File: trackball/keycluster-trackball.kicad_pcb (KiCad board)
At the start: 2 copper layers, 15 x 13.2 mm, 7 parts, among them P8 CONN_7, U1 TLE4964-5M, U2 TLE4964-5M, U3 TLE4964-5M, U4 TLE4964-5M

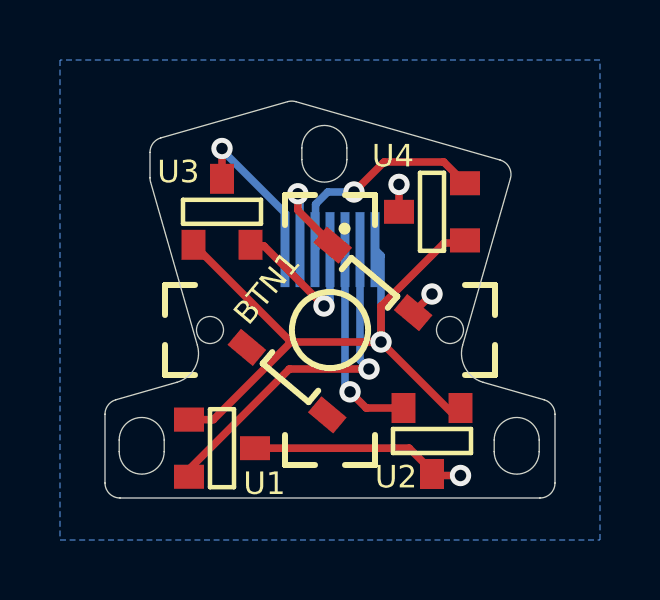
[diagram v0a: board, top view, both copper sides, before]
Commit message: Replace the TL3315NF250Q module with TL3315NFxxxQ and use TL3315NF100Q as the part value to describe the actual part name.
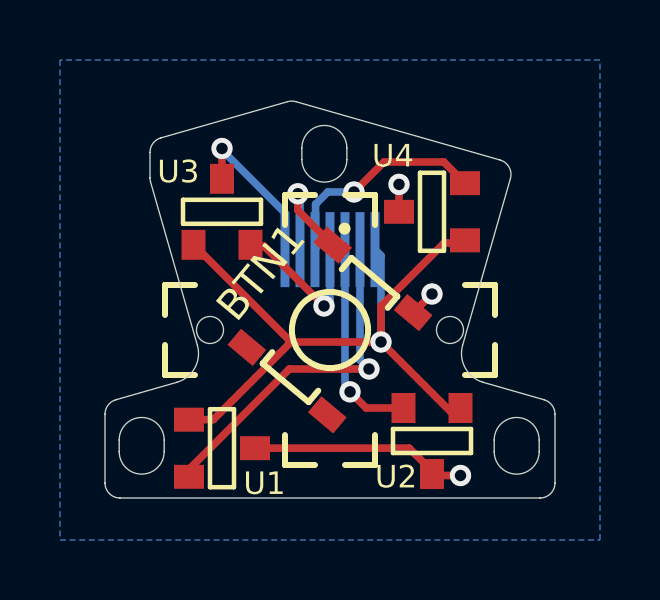
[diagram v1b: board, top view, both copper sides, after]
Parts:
- BTN1: value BTN -> TL3315NF100Q; footprint UGL:TL3315NF250Q -> UGL:TL3315NFxxxQ
- U1, U2, U3, U4: value TLE4964-5M -> TLE49681MXTSA1
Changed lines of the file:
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@@
       (effects (font (size 0.75 0.75) (thickness 0.15)))
     )
-    (fp_text value TLE4964-5M (at 0 -2.667) (layer F.SilkS) hide
+    (fp_text value TLE49681MXTSA1 (at 0 -2.667) (layer F.SilkS) hide
       (effects (font (size 0.75 0.75) (thickness 0.15)))
     )
+    (fp_line (start -1.3 0.4) (end 1.3 0.4) (layer F.SilkS) (width 0.15))
+    (fp_line (start 1.3 -0.4) (end -1.3 -0.4) (layer F.SilkS) (width 0.15))
+    (fp_line (start 1.3 -0.4) (end 1.3 0.4) (layer F.SilkS) (width 0.15))
     (fp_line (start -1.3 -0.4) (end -1.3 0.4) (layer F.SilkS) (width 0.15))
-    (fp_line (start 1.3 -0.4) (end 1.3 0.4) (layer F.SilkS) (width 0.15))
-    (fp_line (start 1.3 -0.4) (end -1.3 -0.4) (layer F.SilkS) (width 0.15))
-    (fp_line (start -1.3 0.4) (end 1.3 0.4) (layer F.SilkS) (width 0.15))
     (pad 1 smd rect (at -0.9525 1.09982) (size 0.8001 1.00076) (layers F.Cu F.Paste F.Mask)
       (net 4 +3V3))
@@
       (effects (font (size 0.75 0.75) (thickness 0.15)))
     )
-    (fp_text value TLE4964-5M (at 0 -2.667 90) (layer F.SilkS) hide
+    (fp_text value TLE49681MXTSA1 (at 0 -2.667 90) (layer F.SilkS) hide
       (effects (font (size 0.75 0.75) (thickness 0.15)))
     )
+    (fp_line (start -1.3 0.4) (end 1.3 0.4) (layer F.SilkS) (width 0.15))
+    (fp_line (start 1.3 -0.4) (end -1.3 -0.4) (layer F.SilkS) (width 0.15))
+    (fp_line (start 1.3 -0.4) (end 1.3 0.4) (layer F.SilkS) (width 0.15))
     (fp_line (start -1.3 -0.4) (end -1.3 0.4) (layer F.SilkS) (width 0.15))
-    (fp_line (start 1.3 -0.4) (end 1.3 0.4) (layer F.SilkS) (width 0.15))
-    (fp_line (start 1.3 -0.4) (end -1.3 -0.4) (layer F.SilkS) (width 0.15))
-    (fp_line (start -1.3 0.4) (end 1.3 0.4) (layer F.SilkS) (width 0.15))
     (pad 1 smd rect (at -0.9525 1.09982 90) (size 0.8001 1.00076) (layers F.Cu F.Paste F.Mask)
       (net 4 +3V3))
@@
       (effects (font (size 0.75 0.75) (thickness 0.15)))
     )
-    (fp_text value TLE4964-5M (at 0 -2.667) (layer F.SilkS) hide
+    (fp_text value TLE49681MXTSA1 (at 0 -2.667) (layer F.SilkS) hide
       (effects (font (size 0.75 0.75) (thickness 0.15)))
     )
+    (fp_line (start -1.3 0.4) (end 1.3 0.4) (layer F.SilkS) (width 0.15))
+    (fp_line (start 1.3 -0.4) (end -1.3 -0.4) (layer F.SilkS) (width 0.15))
+    (fp_line (start 1.3 -0.4) (end 1.3 0.4) (layer F.SilkS) (width 0.15))
     (fp_line (start -1.3 -0.4) (end -1.3 0.4) (layer F.SilkS) (width 0.15))
-    (fp_line (start 1.3 -0.4) (end 1.3 0.4) (layer F.SilkS) (width 0.15))
-    (fp_line (start 1.3 -0.4) (end -1.3 -0.4) (layer F.SilkS) (width 0.15))
-    (fp_line (start -1.3 0.4) (end 1.3 0.4) (layer F.SilkS) (width 0.15))
     (pad 1 smd rect (at -0.9525 1.09982 180) (size 0.8001 1.00076) (layers F.Cu F.Paste F.Mask)
       (net 4 +3V3))
@@
       (effects (font (size 0.75 0.75) (thickness 0.15)))
     )
-    (fp_text value TLE4964-5M (at 0 -2.667 90) (layer F.SilkS) hide
+    (fp_text value TLE49681MXTSA1 (at 0 -2.667 90) (layer F.SilkS) hide
       (effects (font (size 0.75 0.75) (thickness 0.15)))
     )
+    (fp_line (start -1.3 -0.4) (end -1.3 0.4) (layer F.SilkS) (width 0.15))
+    (fp_line (start 1.3 -0.4) (end 1.3 0.4) (layer F.SilkS) (width 0.15))
+    (fp_line (start 1.3 -0.4) (end -1.3 -0.4) (layer F.SilkS) (width 0.15))
     (fp_line (start -1.3 0.4) (end 1.3 0.4) (layer F.SilkS) (width 0.15))
-    (fp_line (start 1.3 -0.4) (end -1.3 -0.4) (layer F.SilkS) (width 0.15))
-    (fp_line (start 1.3 -0.4) (end 1.3 0.4) (layer F.SilkS) (width 0.15))
-    (fp_line (start -1.3 -0.4) (end -1.3 0.4) (layer F.SilkS) (width 0.15))
     (pad 3 smd rect (at 0 -1.09982 270) (size 0.8001 1.00076) (layers F.Cu F.Paste F.Mask)
       (net 1 GND))
@@
       (effects (font (size 1 1) (thickness 0.15)))
     )
+    (fp_circle (center 0 0) (end 1.5 0) (layer Cmts.User) (width 0.2))
+    (fp_line (start 1.5 -4.5) (end -1.5 -4.5) (layer Cmts.User) (width 0.2))
+    (fp_line (start -1.5 -4.5) (end -1.5 -1.5) (layer Cmts.User) (width 0.2))
+    (fp_line (start -1.5 -1.5) (end -5.5 -1.5) (layer Cmts.User) (width 0.2))
+    (fp_line (start -5.5 -1.5) (end -5.5 1.5) (layer Cmts.User) (width 0.2))
+    (fp_line (start -5.5 1.5) (end -1.5 1.5) (layer Cmts.User) (width 0.2))
+    (fp_line (start -1.5 1.5) (end -1.5 4.5) (layer Cmts.User) (width 0.2))
+    (fp_line (start -1.5 4.5) (end 1.5 4.5) (layer Cmts.User) (width 0.2))
+    (fp_line (start 1.5 4.5) (end 1.5 1.5) (layer Cmts.User) (width 0.2))
+    (fp_line (start 1.5 1.5) (end 5.5 1.5) (layer Cmts.User) (width 0.2))
+    (fp_line (start 5.5 1.5) (end 5.5 -1.5) (layer Cmts.User) (width 0.2))
+    (fp_line (start 5.5 -1.5) (end 1.5 -1.5) (layer Cmts.User) (width 0.2))
+    (fp_line (start 1.5 -1.5) (end 1.5 -4.5) (layer Cmts.User) (width 0.2))
+    (fp_line (start -1.5 -3) (end -2 -3) (layer Cmts.User) (width 0.2))
+    (fp_line (start -1.5 -4) (end -2 -4) (layer Cmts.User) (width 0.2))
+    (fp_line (start 1.5 4) (end 2 4) (layer Cmts.User) (width 0.2))
+    (fp_line (start 1.5 3) (end 2 3) (layer Cmts.User) (width 0.2))
+    (fp_line (start 3 -1.5) (end 3 -2) (layer Cmts.User) (width 0.2))
+    (fp_line (start 4 -1.5) (end 4 -2) (layer Cmts.User) (width 0.2))
+    (fp_line (start -3 1.5) (end -3 2) (layer Cmts.User) (width 0.2))
+    (fp_line (start -4 1.5) (end -4 2) (layer Cmts.User) (width 0.2))
+    (fp_line (start -5.5 -1.5) (end -4.5 -1.5) (layer F.SilkS) (width 0.2))
+    (fp_line (start -5.5 -0.5) (end -5.5 -1.5) (layer F.SilkS) (width 0.2))
+    (fp_line (start -5.5 1.5) (end -5.5 0.5) (layer F.SilkS) (width 0.2))
+    (fp_line (start -4.5 1.5) (end -5.5 1.5) (layer F.SilkS) (width 0.2))
+    (fp_line (start 5.5 1.5) (end 4.5 1.5) (layer F.SilkS) (width 0.2))
+    (fp_line (start 5.5 0.5) (end 5.5 1.5) (layer F.SilkS) (width 0.2))
+    (fp_line (start -1.5 -4.5) (end -0.5 -4.5) (layer F.SilkS) (width 0.2))
+    (fp_line (start -1.5 -3.5) (end -1.5 -4.5) (layer F.SilkS) (width 0.2))
+    (fp_line (start 1.5 -4.5) (end 1.5 -3.5) (layer F.SilkS) (width 0.2))
+    (fp_line (start 0.5 -4.5) (end 1.5 -4.5) (layer F.SilkS) (width 0.2))
+    (fp_line (start 5.5 -1.5) (end 5.5 -0.5) (layer F.SilkS) (width 0.2))
+    (fp_line (start 4.5 -1.5) (end 5.5 -1.5) (layer F.SilkS) (width 0.2))
+    (fp_line (start -1.5 4.5) (end -1.5 3.5) (layer F.SilkS) (width 0.2))
+    (fp_line (start -0.5 4.5) (end -1.5 4.5) (layer F.SilkS) (width 0.2))
+    (fp_line (start 1.5 4.5) (end 0.5 4.5) (layer F.SilkS) (width 0.2))
     (fp_line (start 1.5 3.5) (end 1.5 4.5) (layer F.SilkS) (width 0.2))
-    (fp_line (start 1.5 4.5) (end 0.5 4.5) (layer F.SilkS) (width 0.2))
-    (fp_line (start -0.5 4.5) (end -1.5 4.5) (layer F.SilkS) (width 0.2))
-    (fp_line (start -1.5 4.5) (end -1.5 3.5) (layer F.SilkS) (width 0.2))
-    (fp_line (start 4.5 -1.5) (end 5.5 -1.5) (layer F.SilkS) (width 0.2))
-    (fp_line (start 5.5 -1.5) (end 5.5 -0.5) (layer F.SilkS) (width 0.2))
-    (fp_line (start 0.5 -4.5) (end 1.5 -4.5) (layer F.SilkS) (width 0.2))
-    (fp_line (start 1.5 -4.5) (end 1.5 -3.5) (layer F.SilkS) (width 0.2))
-    (fp_line (start -1.5 -3.5) (end -1.5 -4.5) (layer F.SilkS) (width 0.2))
-    (fp_line (start -1.5 -4.5) (end -0.5 -4.5) (layer F.SilkS) (width 0.2))
-    (fp_line (start 5.5 0.5) (end 5.5 1.5) (layer F.SilkS) (width 0.2))
-    (fp_line (start 5.5 1.5) (end 4.5 1.5) (layer F.SilkS) (width 0.2))
-    (fp_line (start -4.5 1.5) (end -5.5 1.5) (layer F.SilkS) (width 0.2))
-    (fp_line (start -5.5 1.5) (end -5.5 0.5) (layer F.SilkS) (width 0.2))
-    (fp_line (start -5.5 -0.5) (end -5.5 -1.5) (layer F.SilkS) (width 0.2))
-    (fp_line (start -5.5 -1.5) (end -4.5 -1.5) (layer F.SilkS) (width 0.2))
-    (fp_line (start -4 1.5) (end -4 2) (layer Cmts.User) (width 0.2))
-    (fp_line (start -3 1.5) (end -3 2) (layer Cmts.User) (width 0.2))
-    (fp_line (start 4 -1.5) (end 4 -2) (layer Cmts.User) (width 0.2))
-    (fp_line (start 3 -1.5) (end 3 -2) (layer Cmts.User) (width 0.2))
-    (fp_line (start 1.5 3) (end 2 3) (layer Cmts.User) (width 0.2))
-    (fp_line (start 1.5 4) (end 2 4) (layer Cmts.User) (width 0.2))
-    (fp_line (start -1.5 -4) (end -2 -4) (layer Cmts.User) (width 0.2))
-    (fp_line (start -1.5 -3) (end -2 -3) (layer Cmts.User) (width 0.2))
-    (fp_line (start 1.5 -1.5) (end 1.5 -4.5) (layer Cmts.User) (width 0.2))
-    (fp_line (start 5.5 -1.5) (end 1.5 -1.5) (layer Cmts.User) (width 0.2))
-    (fp_line (start 5.5 1.5) (end 5.5 -1.5) (layer Cmts.User) (width 0.2))
-    (fp_line (start 1.5 1.5) (end 5.5 1.5) (layer Cmts.User) (width 0.2))
-    (fp_line (start 1.5 4.5) (end 1.5 1.5) (layer Cmts.User) (width 0.2))
-    (fp_line (start -1.5 4.5) (end 1.5 4.5) (layer Cmts.User) (width 0.2))
-    (fp_line (start -1.5 1.5) (end -1.5 4.5) (layer Cmts.User) (width 0.2))
-    (fp_line (start -5.5 1.5) (end -1.5 1.5) (layer Cmts.User) (width 0.2))
-    (fp_line (start -5.5 -1.5) (end -5.5 1.5) (layer Cmts.User) (width 0.2))
-    (fp_line (start -1.5 -1.5) (end -5.5 -1.5) (layer Cmts.User) (width 0.2))
-    (fp_line (start -1.5 -4.5) (end -1.5 -1.5) (layer Cmts.User) (width 0.2))
-    (fp_line (start 1.5 -4.5) (end -1.5 -4.5) (layer Cmts.User) (width 0.2))
-    (fp_circle (center 0 0) (end 1.5 0) (layer Cmts.User) (width 0.2))
     (pad "" np_thru_hole circle (at 4 0) (size 0.9 0.9) (drill 0.9) (layers *.Cu *.Mask))
     (pad "" np_thru_hole circle (at -4 0) (size 0.9 0.9) (drill 0.9) (layers *.Cu *.Mask))
   )
-  (module UGL:TL3315NF250Q locked (layer F.Cu)
+  (module UGL:TL3315NFxxxQ locked (layer F.Cu)
     (at 200 150 50)
-    (fp_text reference BTN1 (at -0.277392 -2.508596 50) (layer F.SilkS)
-      (effects (font (size 0.75 0.75) (thickness 0.15)))
-    )
-    (fp_text value BTN (at 0 3.1 50) (layer F.Fab)
+    (fp_text reference BTN1 (at 0 -3 50) (layer F.SilkS)
       (effects (font (size 1 1) (thickness 0.15)))
     )
+    (fp_text value TL3315NF100Q (at 0 3.1 50) (layer F.Fab)
+      (effects (font (size 1 1) (thickness 0.15)))
+    )
